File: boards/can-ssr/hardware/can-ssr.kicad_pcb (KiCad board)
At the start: 2 copper layers, 100 x 100 mm, 6 parts

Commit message: can-ssr: PCB synced from schematic; return bar on the bottom side
- tools/sync_pcb.py: update a board's PCB from its schematic (adds and
  links footprints, updates fields and nets, never deletes)
- can-ssr: all 123 footprints added (parked off the outline), parity clean
- Fix duplicate R40 (display RSET is now R50)
- Requirements: return bar bolted on the bottom side, bolt order
  S+ S- L- L+, via ring at S-/L-, single-point GND_LOAD

Co-Authored-By: Claude Opus 5.5 <noreply@anthropic.com>
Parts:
- added C1: 10uF 25V X7R, Capacitor_SMD:C_1206_3216Metric_Pad1.33x1.80mm_HandSolder, F.Cu at (220.0, 100.0)
- added C10: 68nF 630V X7R, Capacitor_SMD:C_1210_3225Metric_Pad1.33x2.70mm_HandSolder, F.Cu at (245.0, 100.0)
- added C11: 100nF 50V X7R, Capacitor_SMD:C_0805_2012Metric_Pad1.18x1.45mm_HandSolder, F.Cu at (270.0, 100.0)
- added C2: 10uF 25V X7R, Capacitor_SMD:C_1206_3216Metric_Pad1.33x1.80mm_HandSolder, F.Cu at (295.0, 100.0)
- added C20: 100nF 50V X7R, Capacitor_SMD:C_0805_2012Metric_Pad1.18x1.45mm_HandSolder, F.Cu at (320.0, 100.0)
- added C21: 1nF 50V C0G, Capacitor_SMD:C_1206_3216Metric_Pad1.33x1.80mm_HandSolder, F.Cu at (345.0, 100.0)
- added C22: 100nF 50V X7R, Capacitor_SMD:C_0805_2012Metric_Pad1.18x1.45mm_HandSolder, F.Cu at (370.0, 100.0)
- added C23: 100nF 50V X7R, Capacitor_SMD:C_0805_2012Metric_Pad1.18x1.45mm_HandSolder, F.Cu at (395.0, 100.0)
- added C3: 100nF 50V X7R, Capacitor_SMD:C_0805_2012Metric_Pad1.18x1.45mm_HandSolder, F.Cu at (420.0, 100.0)
- added C30: 10uF 25V X7R, Capacitor_SMD:C_1206_3216Metric_Pad1.33x1.80mm_HandSolder, F.Cu at (445.0, 100.0)
- added C31: 100nF 50V X7R, Capacitor_SMD:C_0805_2012Metric_Pad1.18x1.45mm_HandSolder, F.Cu at (220.0, 125.0)
- added C32: 10uF 25V X7R, Capacitor_SMD:C_1206_3216Metric_Pad1.33x1.80mm_HandSolder, F.Cu at (245.0, 125.0)
- added C33: 100nF 50V X7R, Capacitor_SMD:C_0805_2012Metric_Pad1.18x1.45mm_HandSolder, F.Cu at (270.0, 125.0)
- added C34: 100nF 50V X7R, Capacitor_SMD:C_0805_2012Metric_Pad1.18x1.45mm_HandSolder, F.Cu at (295.0, 125.0)
- added C35: 100nF 50V X7R, Capacitor_SMD:C_0805_2012Metric_Pad1.18x1.45mm_HandSolder, F.Cu at (320.0, 125.0)
- added C36: 100nF 50V X7R, Capacitor_SMD:C_0805_2012Metric_Pad1.18x1.45mm_HandSolder, F.Cu at (345.0, 125.0)
- added C37: 470nF 50V X7R, Capacitor_SMD:C_1206_3216Metric_Pad1.33x1.80mm_HandSolder, F.Cu at (370.0, 125.0)
- added C38: 470nF 50V X7R, Capacitor_SMD:C_1206_3216Metric_Pad1.33x1.80mm_HandSolder, F.Cu at (395.0, 125.0)
- added C4: 100nF 50V X7R, Capacitor_SMD:C_0805_2012Metric_Pad1.18x1.45mm_HandSolder, F.Cu at (420.0, 125.0)
- added C40: 100nF 50V X7R, Capacitor_SMD:C_0805_2012Metric_Pad1.18x1.45mm_HandSolder, F.Cu at (445.0, 125.0)
- added C41: 100nF 50V X7R, Capacitor_SMD:C_0805_2012Metric_Pad1.18x1.45mm_HandSolder, F.Cu at (220.0, 150.0)
- added C42: 100nF 50V X7R, Capacitor_SMD:C_0805_2012Metric_Pad1.18x1.45mm_HandSolder, F.Cu at (245.0, 150.0)
- added C43: 100nF 50V X7R, Capacitor_SMD:C_0805_2012Metric_Pad1.18x1.45mm_HandSolder, F.Cu at (270.0, 150.0)
- added C44: 10uF 25V X7R, Capacitor_SMD:C_1206_3216Metric_Pad1.33x1.80mm_HandSolder, F.Cu at (295.0, 150.0)
- added C5: 100nF 50V X7R, Capacitor_SMD:C_0805_2012Metric_Pad1.18x1.45mm_HandSolder, F.Cu at (320.0, 150.0)
- added C6: 100nF 50V X7R, Capacitor_SMD:C_0805_2012Metric_Pad1.18x1.45mm_HandSolder, F.Cu at (345.0, 150.0)
- added C7: 10uF 25V X7R, Capacitor_SMD:C_1206_3216Metric_Pad1.33x1.80mm_HandSolder, F.Cu at (370.0, 150.0)
- added C8: 27pF 50V C0G, Capacitor_SMD:C_0805_2012Metric_Pad1.18x1.45mm_HandSolder, F.Cu at (395.0, 150.0)
- added C9: 27pF 50V C0G, Capacitor_SMD:C_0805_2012Metric_Pad1.18x1.45mm_HandSolder, F.Cu at (420.0, 150.0)
- added D1: B340A, Diode_SMD:D_SMA_Handsoldering, F.Cu at (445.0, 150.0)
- added D10: SMAZ15, Diode_SMD:D_SMA_Handsoldering, F.Cu at (220.0, 175.0)
- added D11: 1N4148W, Diode_SMD:D_SOD-123, F.Cu at (245.0, 175.0)
- added D12: ES1J, Diode_SMD:D_SMA_Handsoldering, F.Cu at (270.0, 175.0)
- added D13: ES3J, Diode_SMD:D_SMC_Handsoldering, F.Cu at (295.0, 175.0)
- added D2: SMBJ15A, Diode_SMD:D_SMB_Handsoldering, F.Cu at (320.0, 175.0)
- added D20: BAT54, Package_TO_SOT_SMD:SOT-23, F.Cu at (345.0, 175.0)
- added D3: NUP2105L, Package_TO_SOT_SMD:SOT-23, F.Cu at (370.0, 175.0)
- added D4: LED green, LED_SMD:LED_1206_3216Metric_Pad1.42x1.75mm_HandSolder, F.Cu at (395.0, 175.0)
- added D40: LED green, LED_SMD:LED_1206_3216Metric_Pad1.42x1.75mm_HandSolder, F.Cu at (420.0, 175.0)
- added D41: LED green, LED_SMD:LED_1206_3216Metric_Pad1.42x1.75mm_HandSolder, F.Cu at (445.0, 175.0)
- added D5: LED red, LED_SMD:LED_1206_3216Metric_Pad1.42x1.75mm_HandSolder, F.Cu at (220.0, 200.0)
- added H1: SUPPLY +, MountingHole:MountingHole_5.3mm_M5_Pad, F.Cu at (245.0, 200.0)
- added H2: SUPPLY -, MountingHole:MountingHole_5.3mm_M5_Pad, F.Cu at (270.0, 200.0)
- added H3: LOAD +, MountingHole:MountingHole_5.3mm_M5_Pad, F.Cu at (295.0, 200.0)
- added H4: LOAD -, MountingHole:MountingHole_5.3mm_M5_Pad, F.Cu at (320.0, 200.0)
- added J1: CAN IN, Connector_Phoenix_MC:PhoenixContact_MC_1,5_4-G-3.5_1x04_P3.50mm_Horizontal, F.Cu at (345.0, 200.0)
- added J2: CAN OUT, Connector_Phoenix_MC:PhoenixContact_MC_1,5_4-G-3.5_1x04_P3.50mm_Horizontal, F.Cu at (370.0, 200.0)
- added J3: ICSP, Connector_PinHeader_2.54mm:PinHeader_1x06_P2.54mm_Vertical, F.Cu at (395.0, 200.0)
- added J30: MEAN WELL, Connector_Phoenix_MC:PhoenixContact_MC_1,5_5-G-3.5_1x05_P3.50mm_Horizontal, F.Cu at (420.0, 200.0)
- added J4: UART, Connector_PinHeader_2.54mm:PinHeader_1x03_P2.54mm_Vertical, F.Cu at (445.0, 200.0)
- added JP1: TERM, Connector_PinHeader_2.54mm:PinHeader_1x02_P2.54mm_Vertical, F.Cu at (220.0, 225.0)
- added Q1: IPB110N20N3LF, Package_TO_SOT_SMD:TO-263-2, F.Cu at (245.0, 225.0)
- added Q2: IPB110N20N3LF, Package_TO_SOT_SMD:TO-263-2, F.Cu at (270.0, 225.0)
- added Q20: 2N7002, Package_TO_SOT_SMD:SOT-23, F.Cu at (295.0, 225.0)
- added Q21: 2N7002, Package_TO_SOT_SMD:SOT-23, F.Cu at (320.0, 225.0)
- added Q22: 2N7002, Package_TO_SOT_SMD:SOT-23, F.Cu at (345.0, 225.0)
- added Q23: 2N7002, Package_TO_SOT_SMD:SOT-23, F.Cu at (370.0, 225.0)
- added Q24: 2N7002, Package_TO_SOT_SMD:SOT-23, F.Cu at (395.0, 225.0)
- added Q3: IPB110N20N3LF, Package_TO_SOT_SMD:TO-263-2, F.Cu at (420.0, 225.0)
- added Q4: IPB110N20N3LF, Package_TO_SOT_SMD:TO-263-2, F.Cu at (445.0, 225.0)
- added Q5: MMBT2907A, Package_TO_SOT_SMD:SOT-23, F.Cu at (220.0, 250.0)
- added R1: 47k, Resistor_SMD:R_1206_3216Metric_Pad1.30x1.75mm_HandSolder, F.Cu at (245.0, 250.0)
- added R10: 10R, Resistor_SMD:R_1206_3216Metric_Pad1.30x1.75mm_HandSolder, F.Cu at (270.0, 250.0)
- added R11: 10R, Resistor_SMD:R_1206_3216Metric_Pad1.30x1.75mm_HandSolder, F.Cu at (295.0, 250.0)
- added R12: 10R, Resistor_SMD:R_1206_3216Metric_Pad1.30x1.75mm_HandSolder, F.Cu at (320.0, 250.0)
- added R13: 10R, Resistor_SMD:R_1206_3216Metric_Pad1.30x1.75mm_HandSolder, F.Cu at (345.0, 250.0)
- added R14: 10M, Resistor_SMD:R_1206_3216Metric_Pad1.30x1.75mm_HandSolder, F.Cu at (370.0, 250.0)
- added R15: 1M, Resistor_SMD:R_1206_3216Metric_Pad1.30x1.75mm_HandSolder, F.Cu at (395.0, 250.0)
- added R2: 10k, Resistor_SMD:R_1206_3216Metric_Pad1.30x1.75mm_HandSolder, F.Cu at (420.0, 250.0)
- added R20: 16.2k, Resistor_SMD:R_1206_3216Metric_Pad1.30x1.75mm_HandSolder, F.Cu at (445.0, 250.0)
- added R21: 10k, Resistor_SMD:R_1206_3216Metric_Pad1.30x1.75mm_HandSolder, F.Cu at (220.0, 275.0)
- added R22: 1k, Resistor_SMD:R_1206_3216Metric_Pad1.30x1.75mm_HandSolder, F.Cu at (245.0, 275.0)
- added R23: 1k, Resistor_SMD:R_1206_3216Metric_Pad1.30x1.75mm_HandSolder, F.Cu at (270.0, 275.0)
- added R24: 1k, Resistor_SMD:R_1206_3216Metric_Pad1.30x1.75mm_HandSolder, F.Cu at (295.0, 275.0)
- added R25: 10k, Resistor_SMD:R_1206_3216Metric_Pad1.30x1.75mm_HandSolder, F.Cu at (320.0, 275.0)
- added R26: 100k, Resistor_SMD:R_1206_3216Metric_Pad1.30x1.75mm_HandSolder, F.Cu at (345.0, 275.0)
- added R27: 100R, Resistor_SMD:R_1206_3216Metric_Pad1.30x1.75mm_HandSolder, F.Cu at (370.0, 275.0)
- added R28: 100k, Resistor_SMD:R_1206_3216Metric_Pad1.30x1.75mm_HandSolder, F.Cu at (395.0, 275.0)
- added R29: 10k, Resistor_SMD:R_1206_3216Metric_Pad1.30x1.75mm_HandSolder, F.Cu at (420.0, 275.0)
- added R3: 10k, Resistor_SMD:R_1206_3216Metric_Pad1.30x1.75mm_HandSolder, F.Cu at (445.0, 275.0)
- added R30: 4.7k, Resistor_SMD:R_1206_3216Metric_Pad1.30x1.75mm_HandSolder, F.Cu at (220.0, 300.0)
- added R31: 4.7k, Resistor_SMD:R_1206_3216Metric_Pad1.30x1.75mm_HandSolder, F.Cu at (245.0, 300.0)
- added R32: 4.7k, Resistor_SMD:R_1206_3216Metric_Pad1.30x1.75mm_HandSolder, F.Cu at (270.0, 300.0)
- added R33: 4.7k, Resistor_SMD:R_1206_3216Metric_Pad1.30x1.75mm_HandSolder, F.Cu at (295.0, 300.0)
- added R34: 332k, Resistor_SMD:R_1206_3216Metric_Pad1.30x1.75mm_HandSolder, F.Cu at (320.0, 300.0)
- added R35: 332k, Resistor_SMD:R_1206_3216Metric_Pad1.30x1.75mm_HandSolder, F.Cu at (345.0, 300.0)
- added R36: 332k, Resistor_SMD:R_1206_3216Metric_Pad1.30x1.75mm_HandSolder, F.Cu at (370.0, 300.0)
- added R37: 8.06k, Resistor_SMD:R_1206_3216Metric_Pad1.30x1.75mm_HandSolder, F.Cu at (395.0, 300.0)
- added R38: 332k, Resistor_SMD:R_1206_3216Metric_Pad1.30x1.75mm_HandSolder, F.Cu at (420.0, 300.0)
- added R39: 332k, Resistor_SMD:R_1206_3216Metric_Pad1.30x1.75mm_HandSolder, F.Cu at (445.0, 300.0)
- added R4: 10k, Resistor_SMD:R_1206_3216Metric_Pad1.30x1.75mm_HandSolder, F.Cu at (220.0, 325.0)
- added R40: 332k, Resistor_SMD:R_1206_3216Metric_Pad1.30x1.75mm_HandSolder, F.Cu at (245.0, 325.0)
- added R41: 8.06k, Resistor_SMD:R_1206_3216Metric_Pad1.30x1.75mm_HandSolder, F.Cu at (270.0, 325.0)
- added R42: 1k, Resistor_SMD:R_1206_3216Metric_Pad1.30x1.75mm_HandSolder, F.Cu at (295.0, 325.0)
- added R43: 1k, Resistor_SMD:R_1206_3216Metric_Pad1.30x1.75mm_HandSolder, F.Cu at (320.0, 325.0)
- added R44: 20k, Resistor_SMD:R_1206_3216Metric_Pad1.30x1.75mm_HandSolder, F.Cu at (345.0, 325.0)
- added R45: 10k, Resistor_SMD:R_1206_3216Metric_Pad1.30x1.75mm_HandSolder, F.Cu at (370.0, 325.0)
- added R46: 20k, Resistor_SMD:R_1206_3216Metric_Pad1.30x1.75mm_HandSolder, F.Cu at (395.0, 325.0)
- added R47: 10k, Resistor_SMD:R_1206_3216Metric_Pad1.30x1.75mm_HandSolder, F.Cu at (420.0, 325.0)
- added R48: 680R, Resistor_SMD:R_1206_3216Metric_Pad1.30x1.75mm_HandSolder, F.Cu at (445.0, 325.0)
- added R49: 100k, Resistor_SMD:R_1206_3216Metric_Pad1.30x1.75mm_HandSolder, F.Cu at (220.0, 350.0)
- added R5: 120R, Resistor_SMD:R_1206_3216Metric_Pad1.30x1.75mm_HandSolder, F.Cu at (245.0, 350.0)
- added R50: 27k, Resistor_SMD:R_1206_3216Metric_Pad1.30x1.75mm_HandSolder, F.Cu at (270.0, 350.0)
- added R6: 1k, Resistor_SMD:R_1206_3216Metric_Pad1.30x1.75mm_HandSolder, F.Cu at (295.0, 350.0)
- added R7: 1k, Resistor_SMD:R_1206_3216Metric_Pad1.30x1.75mm_HandSolder, F.Cu at (320.0, 350.0)
- added SW1: ADDR, Button_Switch_THT:Nidec_Copal_SH-7010C, F.Cu at (345.0, 350.0)
- added U1: R-78E5.0-1.0, Converter_DCDC:Converter_DCDC_RECOM_R-78E-0.5_THT, F.Cu at (370.0, 350.0)
- added U10: VOM1271T, Thl_Package:Vishay_SOP-4_4.4x4.9mm_P2.54mm_HandSolder, F.Cu at (395.0, 350.0)
- added U11: VOM1271T, Thl_Package:Vishay_SOP-4_4.4x4.9mm_P2.54mm_HandSolder, F.Cu at (420.0, 350.0)
- added U12: ACS770ECB-100U-PFF-T, Sensor_Current:Allegro_CB_PFF, F.Cu at (445.0, 350.0)
- added U2: MCP2562FD-E/P, Package_DIP:DIP-8_W7.62mm_LongPads, F.Cu at (220.0, 375.0)
- added U20: LM393B, Package_SO:SOIC-8_3.9x4.9mm_P1.27mm, F.Cu at (245.0, 375.0)
- added U3: PIC18F47Q84-I/P, Package_DIP:DIP-40_W15.24mm_Socket_LongPads, F.Cu at (270.0, 375.0)
- added U30: UCC12050DVE, Package_SO:SOIC-16W_7.5x10.3mm_P1.27mm, F.Cu at (295.0, 375.0)
- added U31: ISO1640DWR, Package_SO:SOIC-16W_7.5x10.3mm_P1.27mm, F.Cu at (320.0, 375.0)
- added U32: MCP3426A0-E/SN, Package_SO:SOIC-8_3.9x4.9mm_P1.27mm, F.Cu at (345.0, 375.0)
- added U33: MCP4725A0T-E/CH, Package_TO_SOT_SMD:SOT-23-6, F.Cu at (370.0, 375.0)
- added U34: MCP4725A0T-E/CH, Package_TO_SOT_SMD:SOT-23-6, F.Cu at (395.0, 375.0)
- added U35: TLP222A, Package_DIP:DIP-4_W7.62mm_LongPads, F.Cu at (420.0, 375.0)
- added U36: MCP3426A1-E/SN, Package_SO:SOIC-8_3.9x4.9mm_P1.27mm, F.Cu at (445.0, 375.0)
- added U40: MAX7219CWG+, Package_SO:SOIC-24W_7.5x15.4mm_P1.27mm, F.Cu at (220.0, 400.0)
- added U41: CC56-12SRWA, Display_7Segment:CA56-12SRWA, F.Cu at (245.0, 400.0)
- added Y1: 16MHz, Crystal:Crystal_HC49-U_Vertical, F.Cu at (270.0, 400.0)

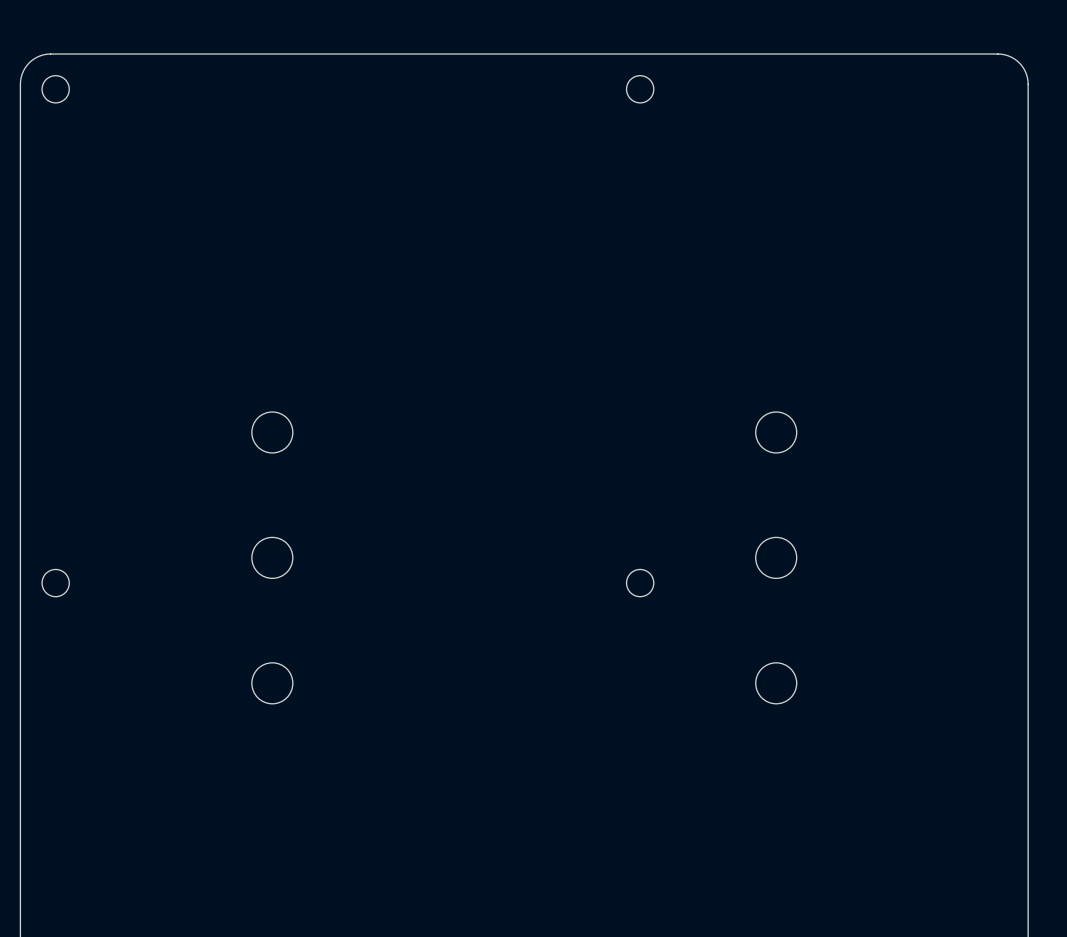
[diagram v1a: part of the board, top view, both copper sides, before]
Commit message: can-ssr: drop Pi holes and DIN clips; 4 x M3 to a mounting plate
- boards/<name>/board.json lets a non-HAT board opt out of the Pi-hole
  rule (rpi_mount: false + reason); check_board.py and CLAUDE.md updated
- can-ssr: Pi M2.5 holes and DIN clip patterns removed; four M3 holes
  (two logic-side corners, two load-side edges with nylon screws) at
  provisional positions; the DIN clips move to a separate plate
- Display stays 0.56 in (requirements note reverted)

Co-Authored-By: Claude Opus 5.5 <noreply@anthropic.com>
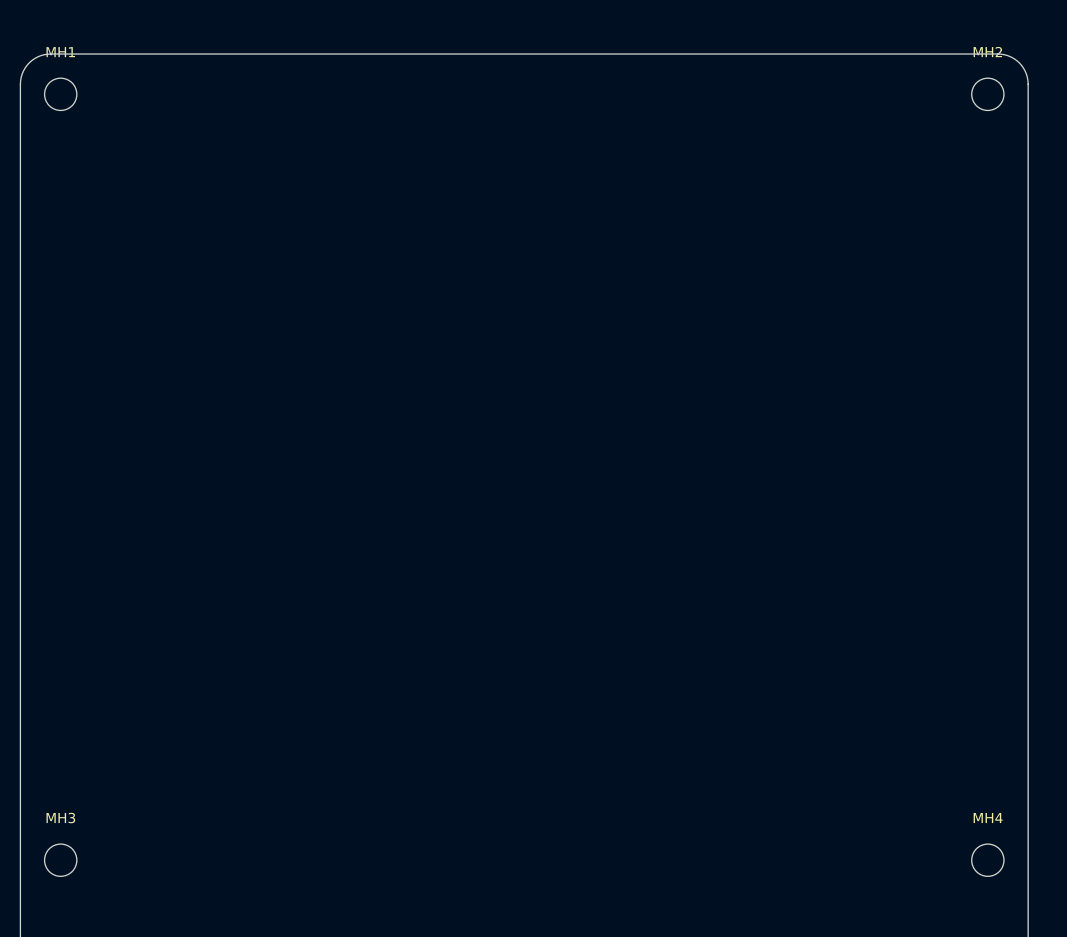
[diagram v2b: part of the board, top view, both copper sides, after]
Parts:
- removed MK1, MK2: DIN_Rail_Mount_3xNPTH4.06mm_P12.45mm, Thl_Mechanical:DIN_Rail_Mount_3xNPTH4.06mm_P12.45mm
- MH1, MH2, MH3, MH4: value MountingHole_2.7mm_M2.5 -> MountingHole_3.2mm_M3; footprint MountingHole:MountingHole_2.7mm_M2.5 -> MountingHole:MountingHole_3.2mm_M3
- moved MH4 44.1 mm to (196.0, 180.0)
- moved MH2 34.5 mm to (196.0, 104.0)
- moved MH3 27.5 mm to (104.0, 180.0)
- moved MH1 0.71 mm to (104.0, 104.0)

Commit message: can-ssr: first-pass placement
All 127 footprints placed: logic half (display, DIP-40 PIC, CAN on the
left edge, MAX7219, R-78E) above a barrier at y ~50-56 straddled by the
VOM1271s, TLP222A, ISO1640, ACS770 and UCC12050; load half below with
the MOSFETs in two columns around the source strip, four M5 bolts on
the bottom edge, J30 on the right edge and the ADC/DAC cluster between
the S- and L- bolts. Trip circuit, PIC decoupling, gate network and
dividers on the bottom side. M3 holes are board-only. No courtyard or
clearance errors; routing not started.

Co-Authored-By: Claude Opus 5.5 <noreply@anthropic.com>
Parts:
- C10, C11, C2, C20, C21, C22, C23, C30, C31, C32, C33, C34, C35, C37, C38, C44, C5, C6, C7, C8, C9, D10, D11, D12, D2, D20, Q20, Q21, Q22, Q23, Q24, Q5, R10, R11, R12, R13, R14, R15, R20, R21, R22, R23, R24, R25, R26, R27, R28, R29, R30, R31, R32, R33, R34, R35, R36, R37, R38, R39, R40, R41, R44, R45, R46, R47, R48, R49, R50, R6, R7, U20: moved to B.Cu
- moved U35 380.4 mm to (114.0, 149.0), turned to -90 degrees
- moved R48 372.9 mm to (119.0, 144.0)
- moved U36 353.7 mm to (140.0, 196.0)
- moved U11 346.5 mm to (135.0, 153.0), turned to -90 degrees
- moved U12 338.0 mm to (174.0, 148.0), turned to 180 degrees
- moved U10 332.6 mm to (127.0, 153.0), turned to -90 degrees
- moved R29 330.7 mm to (123.0, 129.5)
- moved R20 315.0 mm to (154.0, 129.5)
- moved R39 308.1 mm to (163.0, 176.0), turned to 90 degrees
- moved R28 307.9 mm to (120.0, 136.5)
- moved R37 304.4 mm to (117.0, 176.0)
- moved C4 303.2 mm to (117.0, 115.0)
- moved U34 301.2 mm to (155.0, 193.0)
- moved Q4 299.0 mm to (149.7, 178.0)
- moved U41 299.0 mm to (143.1, 118.9), turned to 90 degrees
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
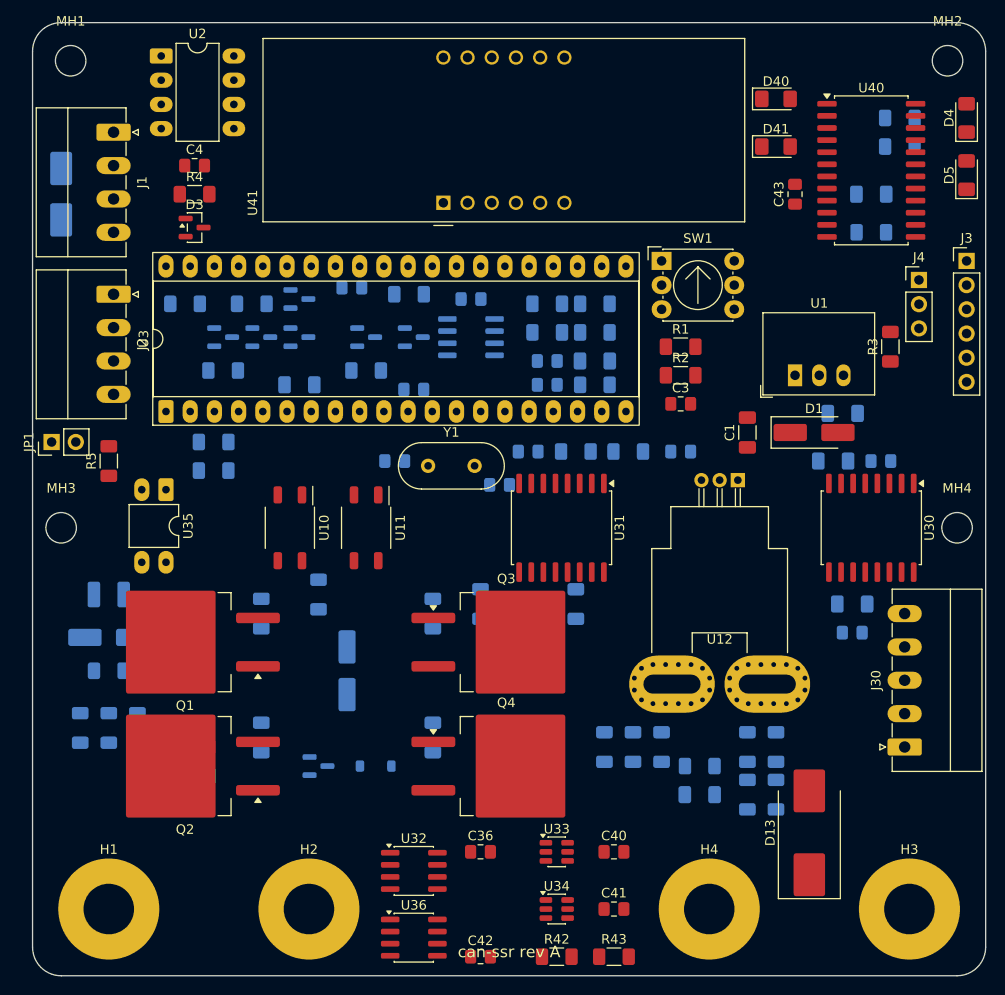
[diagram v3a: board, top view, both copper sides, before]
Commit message: can-ssr: PIC in TQFP-44, barrier moved up, re-placed
- Thl_MCU:PIC18F47Q84-IPT (TQFP-44) symbol from DS40002213C Table 3-2;
  U3 switched from the PDIP-40; schematic regenerated (pins verified)
- sync_pcb.py swaps a footprint in place when the schematic changes it
- Barrier at y ~42-48; ADC cluster in the band under the ISO1640, DACs
  between the ACS770 and J30 (right edge); trip circuit and VOM LED drive
  on the bottom under the display. No courtyard or clearance errors.
- Docs: MCU is now PIC18F47Q84-I/PT

Co-Authored-By: Claude Opus 5.5 <noreply@anthropic.com>
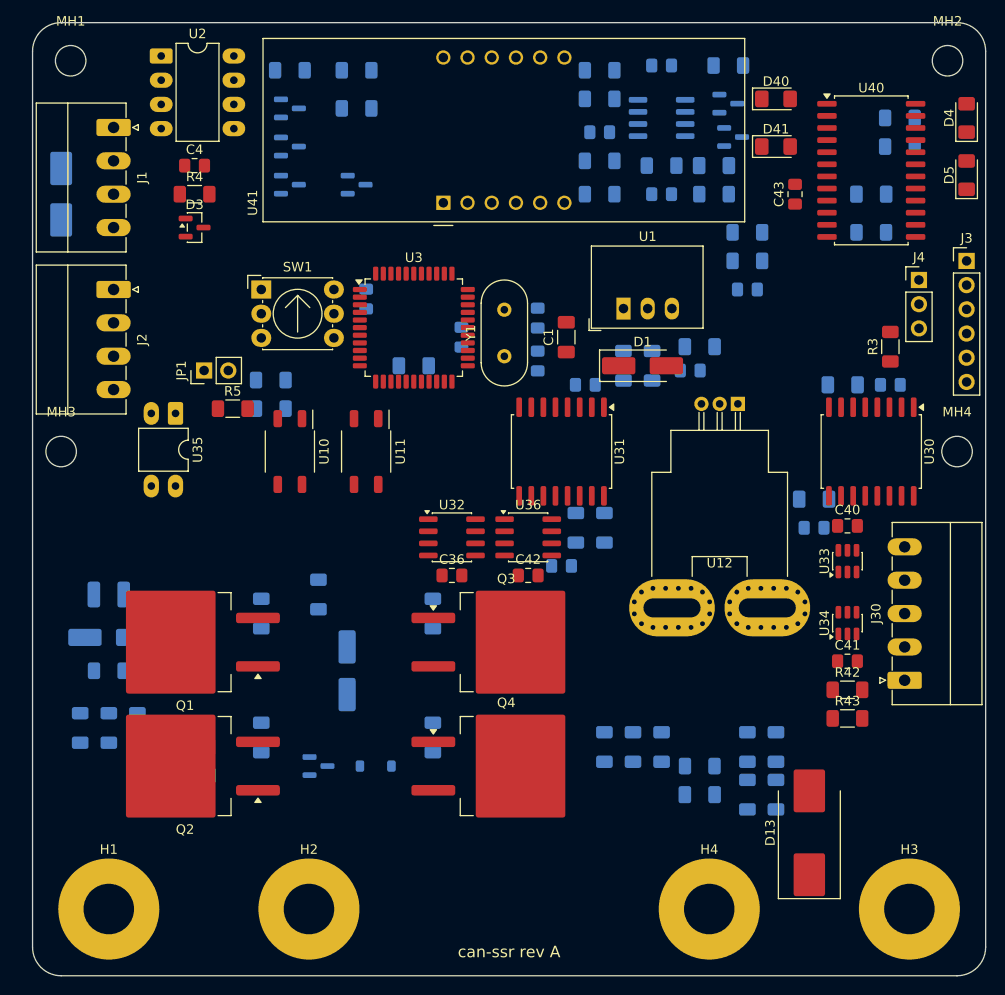
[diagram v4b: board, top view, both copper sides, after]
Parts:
- C3, R1, R2: moved to B.Cu
- U3: value PIC18F47Q84-I/P -> PIC18F47Q84-I/PT; footprint Package_DIP:DIP-40_W15.24mm_Socket_LongPads -> Package_QFP:TQFP-44_10x10mm_P0.8mm
- moved Q20 43.9 mm to (173.5, 112.0)
- moved U36 43.7 mm to (152.0, 154.0)
- moved U33 43.1 mm to (185.5, 156.5), turned to 90 degrees
- moved U34 42.8 mm to (185.5, 163.0), turned to 90 degrees
- moved SW1 42.1 mm to (124.0, 128.0)
- moved C40 42.1 mm to (185.5, 152.8)
- moved R42 41.4 mm to (185.5, 170.0)
- moved R25 41.2 mm to (173.0, 104.5)
- moved D20 41.1 mm to (173.0, 108.5)
- moved C42 40.3 mm to (152.0, 158.0)
- moved C41 35.7 mm to (185.5, 167.0)
- moved U32 35.2 mm to (144.0, 154.0)
- moved R43 35.0 mm to (185.5, 173.0)
- moved R28 34.5 mm to (134.0, 105.0)
- moved C23 31.6 mm to (166.0, 104.5)
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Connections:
- U3 pad 1: /CAN, power, MCU/MCLR -> /CAN, power, MCU/UART_RX
- U3 pad 10: /CAN, power, MCU/LED_FAULT -> /CAN, power, MCU/CAN_TX
- U3 pad 11: +5V -> /CAN, power, MCU/CAN_RX
- U3 pad 12: GND -> unconnected-(U3-NC-Pad12)
- U3 pad 13: /CAN, power, MCU/OSC1 -> unconnected-(U3-NC-Pad13)
- U3 pad 14: /CAN, power, MCU/OSC2 -> /CAN, power, MCU/CAN_STBY
- U3 pad 15: GATE_EN -> unconnected-(U3-RB5-Pad15)
- U3 pad 16: TRIP_OK -> /CAN, power, MCU/ICSPCLK
- U3 pad 17: TRIP_RST -> /CAN, power, MCU/ICSPDAT
- U3 pad 18: I2C_SCL -> /CAN, power, MCU/MCLR
- U3 pad 19: DISP_SCK -> ACS_ADC
- U3 pad 2: ACS_ADC -> /CAN, power, MCU/ADDR0
- U3 pad 20: DISP_DIN -> BUILD_REF
- U3 pad 21: DISP_LOAD -> /CAN, power, MCU/V12_MON
- U3 pad 23: I2C_SDA -> unconnected-(U3-RA4-Pad23)
- U3 pad 25: /CAN, power, MCU/UART_TX -> MW_REMOTE
- U3 pad 26: /CAN, power, MCU/UART_RX -> /CAN, power, MCU/LED_STATUS
- U3 pad 27: /CAN, power, MCU/ADDR0 -> /CAN, power, MCU/LED_FAULT
- U3 pad 28: /CAN, power, MCU/ADDR1 -> +5V
- U3 pad 29: /CAN, power, MCU/ADDR2 -> GND
- U3 pad 3: BUILD_REF -> /CAN, power, MCU/ADDR1
- U3 pad 30: /CAN, power, MCU/ADDR3 -> /CAN, power, MCU/OSC1
- U3 pad 31: GND -> /CAN, power, MCU/OSC2
- U3 pad 32: +5V -> GATE_EN
- U3 pad 35: /CAN, power, MCU/CAN_TX -> TRIP_OK
- U3 pad 36: /CAN, power, MCU/CAN_RX -> TRIP_RST
- U3 pad 37: /CAN, power, MCU/CAN_STBY -> I2C_SCL
- U3 pad 38: unconnected-(U3-RB5-Pad38) -> DISP_SCK
- U3 pad 39: /CAN, power, MCU/ICSPCLK -> DISP_DIN
- U3 pad 4: /CAN, power, MCU/V12_MON -> /CAN, power, MCU/ADDR2
- U3 pad 40: /CAN, power, MCU/ICSPDAT -> DISP_LOAD
- U3 pad 5: unconnected-(U3-RA3-Pad5) -> /CAN, power, MCU/ADDR3
- U3 pad 6: unconnected-(U3-RA4-Pad6) -> GND
- U3 pad 7: unconnected-(U3-RA5-Pad7) -> +5V
- U3 pad 8: MW_REMOTE -> unconnected-(U3-RB0-Pad8)
- U3 pad 9: /CAN, power, MCU/LED_STATUS -> unconnected-(U3-RB1-Pad9)

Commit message: can-ssr: load-side M3 holes moved next to the S+/L+ bolts (nylon)
Co-Authored-By: Claude Opus 5.5 <noreply@anthropic.com>
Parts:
- moved MH3 39.0 mm to (103.0, 184.0)
- moved MH4 39.0 mm to (197.0, 184.0)
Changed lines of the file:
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@@
 	(footprint "MountingHole:MountingHole_3.2mm_M3"
 		(layer "F.Cu")
-		(at 103 145)
+		(at 103 184)
 		(descr "Mounting Hole 3.2mm, M3, no annular, generated by kicad-footprint-generator mountinghole.py")
 		(tags "mountinghole M3")
@@
 	(footprint "MountingHole:MountingHole_3.2mm_M3"
 		(layer "F.Cu")
-		(at 197 145)
+		(at 197 184)
 		(descr "Mounting Hole 3.2mm, M3, no annular, generated by kicad-footprint-generator mountinghole.py")
 		(tags "mountinghole M3")
